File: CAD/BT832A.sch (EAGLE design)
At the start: 43 parts, among them IC1 CP2102, U1 MCP73831T-3ACI/OT, U2 BT832, U3 LP5907MFX-3.3/NOPB, U4 LP5907MFX-3.3/NOPB, U5 ADS131M08IPBS, U6 BCM857BS, X1 ABM3B-8.000MHZ-B2-T, X2 FC-12M

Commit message: edits
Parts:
- added C17: 4.7uF, adafruit:C-USC0402
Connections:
- net GND: now also C17.1
- net NVD: now also C17.2
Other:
- moved on the sheet: C10, C11, C12, C13, C14, C15, C16, D1, D2, D3, IC1, J1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

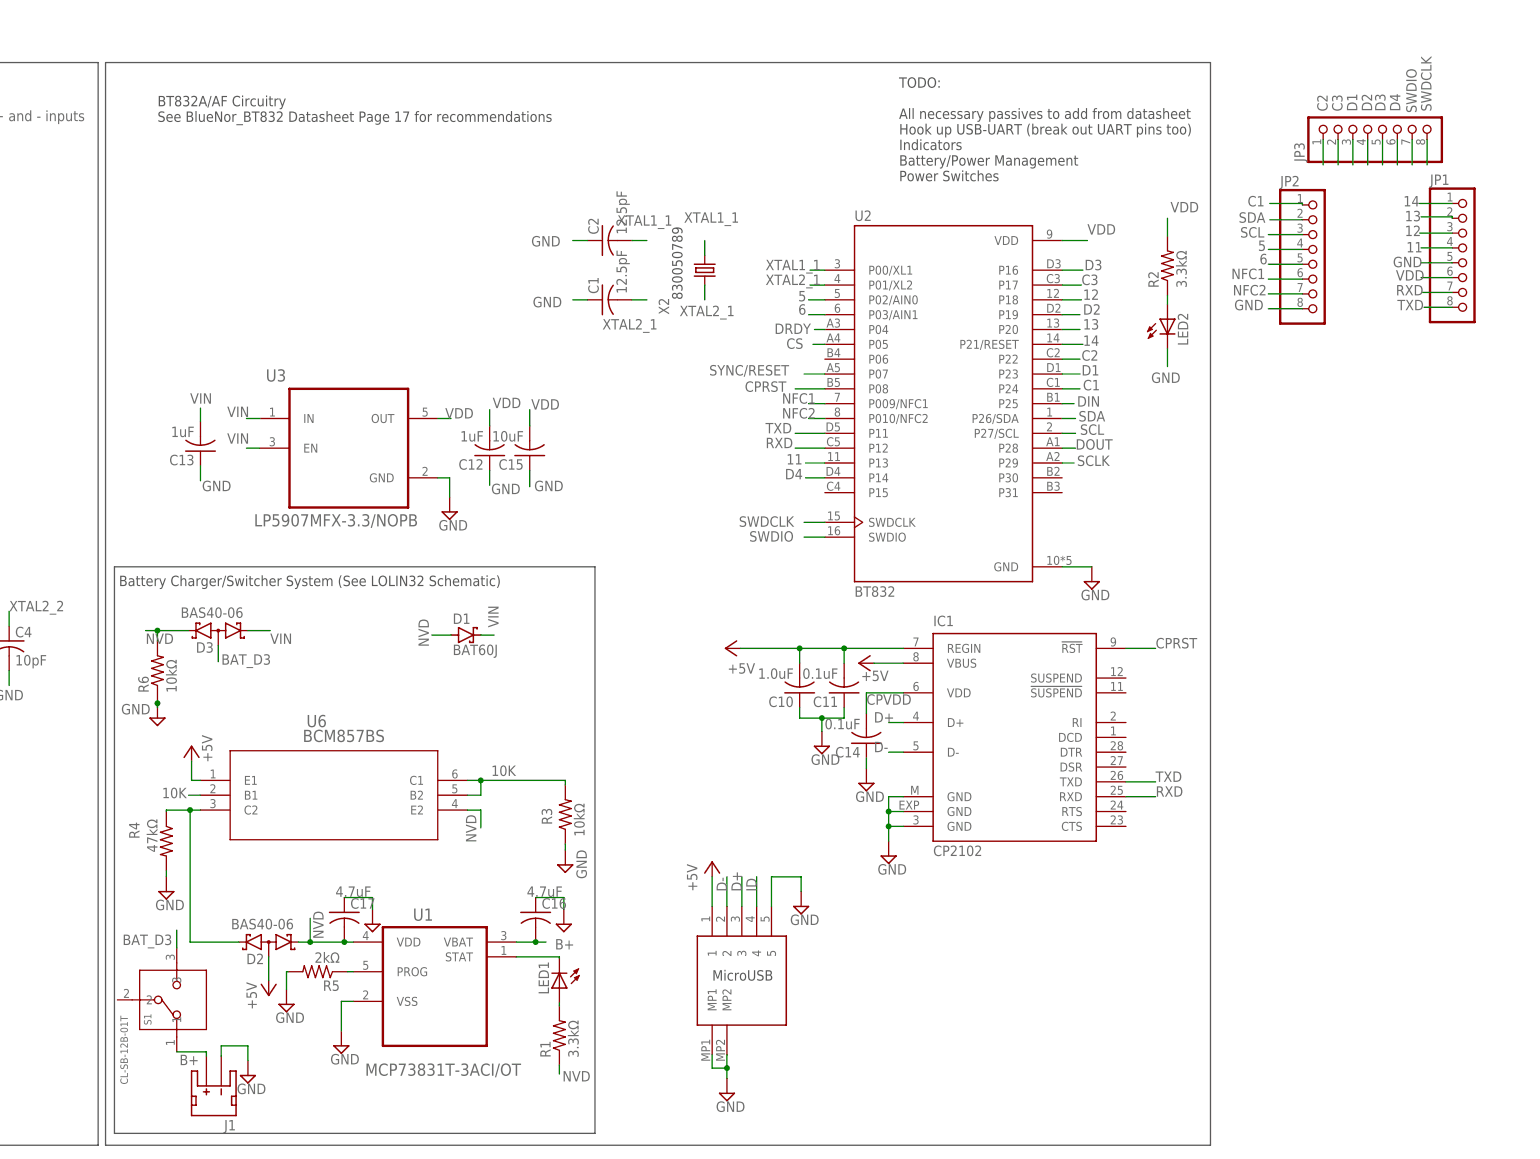
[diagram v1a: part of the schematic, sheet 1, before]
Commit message: replace with 20 pin cp2102
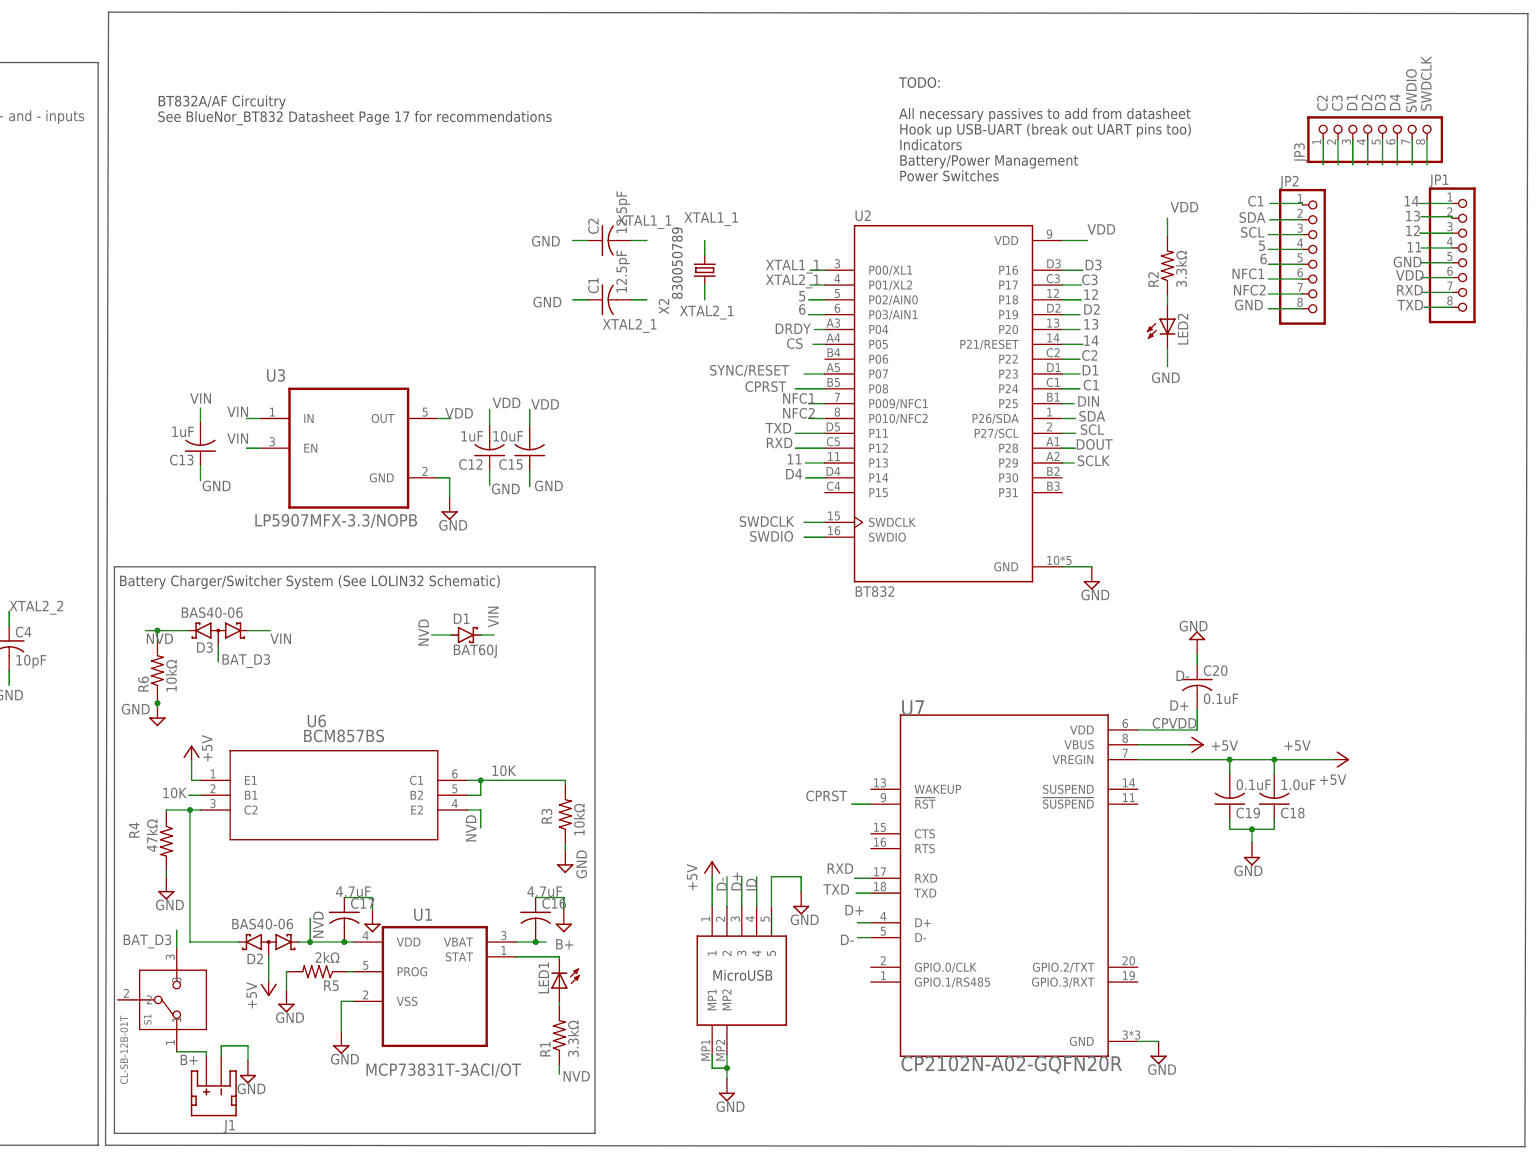
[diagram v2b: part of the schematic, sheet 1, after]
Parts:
- removed C10: 1.0uF, adafruit:C-USC0402
- removed C11, C14: 0.1uF, adafruit:C-USC0402
- removed IC1: CP2102, silabs:CP2102
- added C18: 1.0uF, adafruit:C-USC0402
- added C19, C20: 0.1uF, adafruit:C-USC0402
- added U7: CP2102N-A02-GQFN20R, CP2102N-A02-GQFN20R:CP2102N-A02-GQFN20R
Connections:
- net +5V: now also C18.2, C19.2, U7.VBUS, U7.VREGIN; no longer C10.2, C11.2, IC1.REGIN, IC1.VBUS
- net CPRST: now also U7.!RST; no longer IC1.!RST
- net CPVDD: now also C20.2, U7.VDD; no longer C14.2, IC1.VDD
- net D+: now also U7.D+; no longer IC1.D+
- net D-: now also U7.D-; no longer IC1.D-
- net GND: now also C18.1, C19.1, C20.1, U7.GND; no longer C10.1, C11.1, C14.1, IC1.GND, IC1.GND@EXP, IC1.GND@M
- net RXD: now also U7.RXD; no longer IC1.RXD
- net TXD: now also U7.TXD; no longer IC1.TXD
